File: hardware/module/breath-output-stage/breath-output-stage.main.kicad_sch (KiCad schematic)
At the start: 11 parts

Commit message: WIP module schematics: footprints, bought-part fields, and the two board projects (module-main, module-jack)
Recovered from a container restart; not yet exported or checked.

Co-Authored-By: Claude Opus 5.5 <noreply@anthropic.com>
Claude-Session: https://claude.ai/code/session_01LmB4muFXnoLprWX4JzuJ5A
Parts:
- C-DEC-BREATH-NEG, C-DEC-BREATH-POS: footprint (none) -> Capacitor_SMD:C_0805_2012Metric; Assembly (none) -> machine; LCSC (none) -> C49678; MPN (none) -> CC0805KRX7R9BB104; Manufacturer (none) -> YAGEO
- C-OUT-BREATH: footprint (none) -> Capacitor_SMD:C_1206_3216Metric; Assembly (none) -> machine; LCSC (none) -> C3774076; MPN (none) -> 50MU334MA23216; Manufacturer (none) -> Rubycon
- D-JACK-CLAMP: footprint (none) -> Package_TO_SOT_SMD:SOT-23; Assembly (none) -> machine; LCSC (none) -> C2500; MPN (none) -> BAV99,215; Manufacturer (none) -> Nexperia
- R-BREATH-FB: footprint (none) -> Resistor_SMD:R_0805_2012Metric; Assembly (none) -> machine; LCSC (none) -> C17678; MPN (none) -> 0805W8F4022T5E; Manufacturer (none) -> UNI-ROYAL(Uniroyal Elec)
- R-BREATH-IN: footprint (none) -> Resistor_SMD:R_0805_2012Metric; Assembly (none) -> machine; LCSC (none) -> C17414; MPN (none) -> 0805W8F1002T5E; Manufacturer (none) -> UNI-ROYAL(Uniroyal Elec)
- R-BREATH-OFF: footprint (none) -> Resistor_SMD:R_0805_2012Metric; Assembly (none) -> machine; LCSC (none) -> C17550; MPN (none) -> 0805W8F2102T5E; Manufacturer (none) -> UNI-ROYAL(Uniroyal Elec)
- R-BREATH-OFFNEG: footprint (none) -> Resistor_SMD:R_0805_2012Metric; Assembly (none) -> machine; LCSC (none) -> C17873; MPN (none) -> 0805W8F9532T5E; Manufacturer (none) -> UNI-ROYAL(Uniroyal Elec)
- R-GAIN-FLOOR: footprint (none) -> Resistor_SMD:R_0805_2012Metric; Assembly (none) -> machine; LCSC (none) -> C17806; MPN (none) -> 0805W8F7151T5E; Manufacturer (none) -> UNI-ROYAL(Uniroyal Elec)
- R-OUT-PROT: footprint (none) -> Resistor_SMD:R_1206_3216Metric; Assembly (none) -> machine; LCSC (none) -> C4261071; MPN (none) -> ERJ-P08F1001V; Manufacturer (none) -> Panasonic
- U-BREATH-OPA: footprint (none) -> Package_SO:SOIC-8_3.9x4.9mm_P1.27mm; Assembly (none) -> machine; LCSC (none) -> C139363; MPN (none) -> OPA2197IDR; Manufacturer (none) -> Texas Instruments

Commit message: #32: checkpoint — switchable breath band-limit, 1.5 kHz ADC filter, breath LED
Receive stage: C_diff switched by U-BW-SW (TMUX6112) from SW-BREATH-BW
(NKK M2024, left 500 Hz / centre 1.5 kHz / right WIDE): 680 pF fixed,
3.9 nF and 10 nF switched; C_cm 68 pF matched pair. C-OUT-BREATH 10 nF C0G.
C-AA-ADC 18 nF (1.47 kHz), sample rate kept at 4 kHz. Breath LED driver on
U-REF-BUF B. Sheets, BOM fragments, datasheets (TMUX6112, MMBT3904), sims,
ADR 0003/0004 amendments, pages. Sims still being re-run.

Gate-Red: sims stale while re-running (breath-receive-stage, breath-output-stage, interfaces/system, pitch-stage); breath-sense-link/sim pg_gain_max < 1e-3 fails in every mode and power-entry/sim led-pwm breath_mv fails at 2 kHz - both consequences of #32 left for the owner, not loosened; breath-receive-stage cmrr-wide fails 58.5 dB above ~7.4 kHz (owner); kicad: module-main and main-board .kicad_pcb parity broken by the new/changed parts (re-placement is the module re-layout's; pcb not touched), plus module-main's pre-existing routing failures

Co-Authored-By: Claude Opus 5.5 <noreply@anthropic.com>
Claude-Session: https://claude.ai/code/session_01LmB4muFXnoLprWX4JzuJ5A
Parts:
- C-OUT-BREATH: value 330nF film -> 10nF C0G; LCSC C3774076 -> C97928; MPN 50MU334MA23216 -> GRM3195C1H103JA01D; Manufacturer Rubycon -> Murata
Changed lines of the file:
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@@
     (in_bom yes) (on_board yes) (dnp no)
     (property "Reference" "C-OUT-BREATH" (at 43.18 232.41 0) (effects (font (size 1.27 1.27)) (justify left)))
-    (property "Value" "330nF film" (at 43.18 234.95 0) (effects (font (size 1.27 1.27)) (justify left)))
+    (property "Value" "10nF C0G" (at 43.18 234.95 0) (effects (font (size 1.27 1.27)) (justify left)))
     (property "Footprint" "Capacitor_SMD:C_1206_3216Metric" (at 41.91 237.49 0) (effects (font (size 1.27 1.27)) hide))
     (property "Datasheet" "" (at 40.64 233.68 0) (effects (font (size 1.27 1.27)) hide))
     (property "Row" "C-OUT-BREATH" (at 40.64 233.68 0) (effects (font (size 1.27 1.27)) hide))
     (property "Pins" "1=1 2=2" (at 40.64 233.68 0) (effects (font (size 1.27 1.27)) hide))
-    (property "Manufacturer" "Rubycon" (at 40.64 233.68 0) (effects (font (size 1.27 1.27)) hide))
-    (property "MPN" "50MU334MA23216" (at 40.64 233.68 0) (effects (font (size 1.27 1.27)) hide))
-    (property "LCSC" "C3774076" (at 40.64 233.68 0) (effects (font (size 1.27 1.27)) hide))
+    (property "Manufacturer" "Murata" (at 40.64 233.68 0) (effects (font (size 1.27 1.27)) hide))
+    (property "MPN" "GRM3195C1H103JA01D" (at 40.64 233.68 0) (effects (font (size 1.27 1.27)) hide))
+    (property "LCSC" "C97928" (at 40.64 233.68 0) (effects (font (size 1.27 1.27)) hide))
     (property "Assembly" "machine" (at 40.64 233.68 0) (effects (font (size 1.27 1.27)) hide))
     (pin "1")
@@
   (label "SUM_NODE" (at 81.28 53.34 180) (fields_autoplaced) (effects (font (size 1.27 1.27)) (justify right bottom)))
   (wire (pts (xy 99.06 50.8) (xy 101.6 50.8)) (stroke (width 0) (type default)))
-  (label "BREATH_OUT" (at 101.6 50.8 0) (fields_autoplaced) (effects (font (size 1.27 1.27)) (justify left bottom)))
+  (hierarchical_label "BREATH_OUT" (shape output) (at 101.6 50.8 0) (effects (font (size 1.27 1.27)) (justify left))
+    (property "Dir" "out" (at 101.6 50.8 0) (effects (font (size 1.27 1.27)) hide))
+    (property "To" "module/breath-receive-stage" (at 101.6 50.8 0) (effects (font (size 1.27 1.27)) hide))
+    (property "Note" "The summer's output inside its loop, ahead of R-OUT-PROT: the breath LED's driver reads it (#32)" (at 101.6 50.8 0) (effects (font (size 1.27 1.27)) hide)))
   (wire (pts (xy 345.44 191.77) (xy 345.44 194.31)) (stroke (width 0) (type default)))
-  (label "BREATH_OUT" (at 345.44 194.31 270) (fields_autoplaced) (effects (font (size 1.27 1.27)) (justify right bottom)))
+  (hierarchical_label "BREATH_OUT" (shape output) (at 345.44 194.31 270) (effects (font (size 1.27 1.27)) (justify right))
+    (property "Dir" "out" (at 345.44 194.31 0) (effects (font (size 1.27 1.27)) hide))
+    (property "To" "module/breath-receive-stage" (at 345.44 194.31 0) (effects (font (size 1.27 1.27)) hide))
+    (property "Note" "The summer's output inside its loop, ahead of R-OUT-PROT: the breath LED's driver reads it (#32)" (at 345.44 194.31 0) (effects (font (size 1.27 1.27)) hide)))
   (wire (pts (xy 421.64 193.04) (xy 421.64 195.58)) (stroke (width 0) (type default)))
-  (label "BREATH_OUT" (at 421.64 195.58 270) (fields_autoplaced) (effects (font (size 1.27 1.27)) (justify right bottom)))
+  (hierarchical_label "BREATH_OUT" (shape output) (at 421.64 195.58 270) (effects (font (size 1.27 1.27)) (justify right))
+    (property "Dir" "out" (at 421.64 195.58 0) (effects (font (size 1.27 1.27)) hide))
+    (property "To" "module/breath-receive-stage" (at 421.64 195.58 0) (effects (font (size 1.27 1.27)) hide))
+    (property "Note" "The summer's output inside its loop, ahead of R-OUT-PROT: the breath LED's driver reads it (#32)" (at 421.64 195.58 0) (effects (font (size 1.27 1.27)) hide)))
   (wire (pts (xy 497.84 184.15) (xy 497.84 181.61)) (stroke (width 0) (type default)))
-  (label "BREATH_OUT" (at 497.84 181.61 90) (fields_autoplaced) (effects (font (size 1.27 1.27)) (justify left bottom)))
+  (hierarchical_label "BREATH_OUT" (shape output) (at 497.84 181.61 90) (effects (font (size 1.27 1.27)) (justify left))
+    (property "Dir" "out" (at 497.84 181.61 0) (effects (font (size 1.27 1.27)) hide))
+    (property "To" "module/breath-receive-stage" (at 497.84 181.61 0) (effects (font (size 1.27 1.27)) hide))
+    (property "Note" "The summer's output inside its loop, ahead of R-OUT-PROT: the breath LED's driver reads it (#32)" (at 497.84 181.61 0) (effects (font (size 1.27 1.27)) hide)))
   (wire (pts (xy 497.84 191.77) (xy 497.84 194.31)) (stroke (width 0) (type default)))
   (hierarchical_label "JACK_TIP" (shape passive) (at 497.84 194.31 270) (effects (font (size 1.27 1.27)) (justify right))

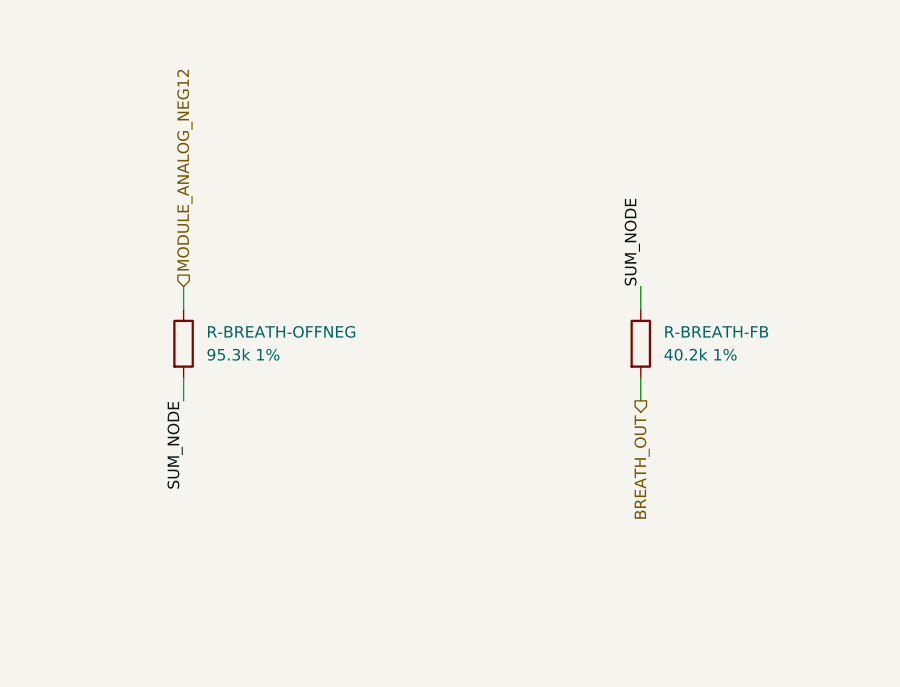
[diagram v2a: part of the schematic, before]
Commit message: #32: checkpoint - the owner's three answers and side-adjust trimmers
Owner decisions of 2026-10-04, recorded in ADR 0003/0004/0023/0024:
- WIDE's CMRR requirement band is DC to 7 kHz ("Keep 10 kHz, accept");
  cmrr-wide holds 58.5 dB there and records 10 kHz.
- D-TVS-BREATH is the PESD12VL1BA (19 pF), datasheet banked; PWR_GND
  held under -60 dB in each mode's band, WIDE at the accepted figure.
- The -12 V offset leg is filtered: R-BREATH-OFFNEG-A/-B 47.5k with
  C-BREATH-OFFNEG 1 uF at the split (6.7 Hz). Rest level +16 mV.
- The four trimmers are Bourns 3296X side-adjust, set with the module
  out of the rack; no rear-access windows. Current 3296 datasheet banked.

Sims are mid-run; their results land in the next commit.

Gate-Red: sim results stale or pre-change for receive-stage, power-entry, pitch-stage, mod-channels, shaper, system, breath-excitation-reference, digital-and-supervision and panel-led while they re-run on these inputs (checkpoint, as asked every 45 min); module-main and main-board .kicad_pcb parity with the new/changed parts (layout's, not touched here); main-board fab stale against the breath-adc sheet; module-main's existing routing/silk/acid-trap failures.

Co-Authored-By: Claude Opus 5.5 <noreply@anthropic.com>
Claude-Session: https://claude.ai/code/session_01LmB4muFXnoLprWX4JzuJ5A
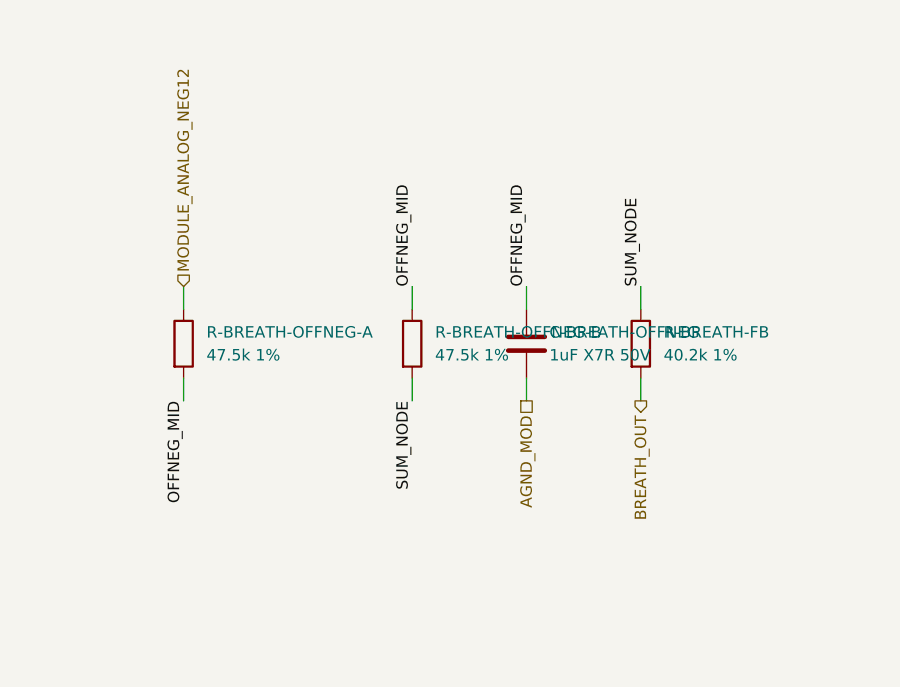
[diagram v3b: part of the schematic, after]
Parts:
- added C-BREATH-OFFNEG: 1uF X7R 50V, Capacitor_SMD:C_1206_3216Metric, symbol Device:C
- added R-BREATH-OFFNEG-B: 47.5k 1%, Resistor_SMD:R_0805_2012Metric, symbol Device:R
- R-BREATH-OFFNEG-A: renamed from R-BREATH-OFFNEG; value 95.3k 1% -> 47.5k 1%; LCSC C17873 -> C26011; MPN 0805W8F9532T5E -> 0805W8F4752T5E
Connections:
- net AGND_MOD: now also C-BREATH-OFFNEG.2
- net SUM_NODE: now also R-BREATH-OFFNEG-B.2; no longer R-BREATH-OFFNEG-A.2
- new net OFFNEG_MID: C-BREATH-OFFNEG.1, R-BREATH-OFFNEG-A.2, R-BREATH-OFFNEG-B.1
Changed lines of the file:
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@@
   (symbol (lib_id "Device:R") (at 294.64 187.96 0) (unit 1)
     (in_bom yes) (on_board yes) (dnp no)
-    (property "Reference" "R-BREATH-OFFNEG" (at 297.18 186.69 0) (effects (font (size 1.27 1.27)) (justify left)))
-    (property "Value" "95.3k 1%" (at 297.18 189.23 0) (effects (font (size 1.27 1.27)) (justify left)))
+    (property "Reference" "R-BREATH-OFFNEG-A" (at 297.18 186.69 0) (effects (font (size 1.27 1.27)) (justify left)))
+    (property "Value" "47.5k 1%" (at 297.18 189.23 0) (effects (font (size 1.27 1.27)) (justify left)))
     (property "Footprint" "Resistor_SMD:R_0805_2012Metric" (at 293.37 187.96 0) (effects (font (size 1.27 1.27)) hide))
     (property "Datasheet" "" (at 294.64 187.96 0) (effects (font (size 1.27 1.27)) hide))
@@
     (property "Drawn_as" "R-OFFNEG" (at 294.64 187.96 0) (effects (font (size 1.27 1.27)) hide))
     (property "Manufacturer" "UNI-ROYAL(Uniroyal Elec)" (at 294.64 187.96 0) (effects (font (size 1.27 1.27)) hide))
-    (property "MPN" "0805W8F9532T5E" (at 294.64 187.96 0) (effects (font (size 1.27 1.27)) hide))
-    (property "LCSC" "C17873" (at 294.64 187.96 0) (effects (font (size 1.27 1.27)) hide))
+    (property "MPN" "0805W8F4752T5E" (at 294.64 187.96 0) (effects (font (size 1.27 1.27)) hide))
+    (property "LCSC" "C26011" (at 294.64 187.96 0) (effects (font (size 1.27 1.27)) hide))
     (property "Assembly" "machine" (at 294.64 187.96 0) (effects (font (size 1.27 1.27)) hide))
     (pin "1")
     (pin "2")
-    (instances (project "module-main" (path "/fc77e9f9-9171-5c83-92ae-8cafe880764e/17312cee-ca35-5de4-93d5-247b1fad2ee3" (reference "R24") (unit 1))) (project "breath-output-stage.main" (path "/1628897f-2ed0-5a6a-9bf2-749dfca7ac5c" (reference "R-BREATH-OFFNEG") (unit 1))) (project "breath-output-stage" (path "/6f4edadb-6257-58e5-9d51-bec8cbdf5df0/ec51b1d2-0ca2-56b1-b291-6e590255992a" (reference "R-BREATH-OFFNEG") (unit 1))))
+    (instances (project "module-main" (path "/fc77e9f9-9171-5c83-92ae-8cafe880764e/17312cee-ca35-5de4-93d5-247b1fad2ee3" (reference "R24") (unit 1))) (project "breath-output-stage.main" (path "/1628897f-2ed0-5a6a-9bf2-749dfca7ac5c" (reference "R-BREATH-OFFNEG-A") (unit 1))) (project "breath-output-stage" (path "/6f4edadb-6257-58e5-9d51-bec8cbdf5df0/ec51b1d2-0ca2-56b1-b291-6e590255992a" (reference "R-BREATH-OFFNEG-A") (unit 1))))
   )
   (symbol (lib_id "Device:R") (at 345.44 187.96 0) (unit 1)
@@
   (label "SUM_NODE" (at 243.84 194.31 270) (fields_autoplaced) (effects (font (size 1.27 1.27)) (justify right bottom)))
   (wire (pts (xy 294.64 191.77) (xy 294.64 194.31)) (stroke (width 0) (type default)))
-  (label "SUM_NODE" (at 294.64 194.31 270) (fields_autoplaced) (effects (font (size 1.27 1.27)) (justify right bottom)))
+  (label "OFFNEG_MID" (at 294.64 194.31 270) (fields_autoplaced) (effects (font (size 1.27 1.27)) (justify right bottom)))
   (wire (pts (xy 345.44 184.15) (xy 345.44 181.61)) (stroke (width 0) (type default)))
   (label "SUM_NODE" (at 345.44 181.61 90) (fields_autoplaced) (effects (font (size 1.27 1.27)) (justify left bottom)))
@@
     (property "Dir" "ref" (at 142.24 194.31 0) (effects (font (size 1.27 1.27)) hide))
     (property "From" "module/power-entry" (at 142.24 194.31 0) (effects (font (size 1.27 1.27)) hide)))
+  (symbol (lib_id "Device:R") (at 320.04 187.96 0) (unit 1)
+    (in_bom yes) (on_board yes) (dnp no)
+    (property "Reference" "R-BREATH-OFFNEG-B" (at 322.58 186.69 0) (effects (font (size 1.27 1.27)) (justify left)))
+    (property "Value" "47.5k 1%" (at 322.58 189.23 0) (effects (font (size 1.27 1.27)) (justify left)))
+    (property "Footprint" "Resistor_SMD:R_0805_2012Metric" (at 318.77 187.96 0) (effects (font (size 1.27 1.27)) hide))
+    (property "Datasheet" "" (at 320.04 187.96 0) (effects (font (size 1.27 1.27)) hide))
+    (property "Row" "R-BREATH-OFFNEG" (at 320.04 187.96 0) (effects (font (size 1.27 1.27)) hide))
+    (property "Pins" "1=1 2=2" (at 320.04 187.96 0) (effects (font (size 1.27 1.27)) hide))
+    (property "Drawn_as" "R-OFFNEG" (at 320.04 187.96 0) (effects (font (size 1.27 1.27)) hide))
+    (property "Note" "The second half of the offset's -12 V leg (#32, owner 2026-10-04: 'Add RC filter (Recommended)'): R-BREATH-OFFNEG-A from -12 V to OFFNEG_MID, this from OFFNEG_MID to the summing node, C-BREATH-OFFNEG from OFFNEG_MID to the star. 2 x 47.5k for the 95.3k it replaces" (at 320.04 187.96 0) (effects (font (size 1.27 1.27)) hide))
+    (property "Pins_source" "Device:R, two-terminal: pin 1 and pin 2 are interchangeable" (at 320.04 187.96 0) (effects (font (size 1.27 1.27)) hide))
+    (property "Manufacturer" "UNI-ROYAL(Uniroyal Elec)" (at 320.04 187.96 0) (effects (font (size 1.27 1.27)) hide))
+    (property "MPN" "0805W8F4752T5E" (at 320.04 187.96 0) (effects (font (size 1.27 1.27)) hide))
+    (property "LCSC" "C26011" (at 320.04 187.96 0) (effects (font (size 1.27 1.27)) hide))
+    (property "Assembly" "machine" (at 320.04 187.96 0) (effects (font (size 1.27 1.27)) hide))
+    (pin "1")
+    (pin "2")
+    (instances (project "breath-output-stage.main" (path "/1628897f-2ed0-5a6a-9bf2-749dfca7ac5c" (reference "R-BREATH-OFFNEG-B") (unit 1))) (project "module-main" (path "/fc77e9f9-9171-5c83-92ae-8cafe880764e/17312cee-ca35-5de4-93d5-247b1fad2ee3" (reference "R82") (unit 1))) (project "breath-output-stage" (path "/6f4edadb-6257-58e5-9d51-bec8cbdf5df0/ec51b1d2-0ca2-56b1-b291-6e590255992a" (reference "R-BREATH-OFFNEG-B") (unit 1))))
+  )
+  (wire (pts (xy 320.04 184.15) (xy 320.04 181.61)) (stroke (width 0) (type default)))
+  (label "OFFNEG_MID" (at 320.04 181.61 90) (fields_autoplaced) (effects (font (size 1.27 1.27)) (justify left bottom)))
+  (wire (pts (xy 320.04 191.77) (xy 320.04 194.31)) (stroke (width 0) (type default)))
+  (label "SUM_NODE" (at 320.04 194.31 270) (fields_autoplaced) (effects (font (size 1.27 1.27)) (justify right bottom)))
+  (symbol (lib_id "Device:C") (at 332.74 187.96 0) (unit 1)
+    (in_bom yes) (on_board yes) (dnp no)
+    (property "Reference" "C-BREATH-OFFNEG" (at 335.28 186.69 0) (effects (font (size 1.27 1.27)) (justify left)))
+    (property "Value" "1uF X7R 50V" (at 335.28 189.23 0) (effects (font (size 1.27 1.27)) (justify left)))
+    (property "Footprint" "Capacitor_SMD:C_1206_3216Metric" (at 334.01 191.77 0) (effects (font (size 1.27 1.27)) hide))
+    (property "Datasheet" "" (at 332.74 187.96 0) (effects (font (size 1.27 1.27)) hide))
+    (property "Row" "C-BREATH-OFFNEG" (at 332.74 187.96 0) (effects (font (size 1.27 1.27)) hide))
+    (property "Pins" "1=1 2=2" (at 332.74 187.96 0) (effects (font (size 1.27 1.27)) hide))
+    (property "Note" "Filters the -12 V rail out of the breath offset (#32): 1/(2 pi x 23.75 kohm x 1 uF) = 6.7 Hz, so the LED row's 2-4 kHz PWM and the rail's breath-rate movement are taken down before the summer. Returns to the star. X7R 50 V in 1206 so 6 V of DC bias costs little; a 1206 C0G at 1 uF is not stocked" (at 332.74 187.96 0) (effects (font (size 1.27 1.27)) hide))
+    (property "Pins_source" "Device:C, two-terminal: pin 1 and pin 2 are interchangeable" (at 332.74 187.96 0) (effects (font (size 1.27 1.27)) hide))
+    (property "Manufacturer" "Samsung Electro-Mechanics" (at 332.74 187.96 0) (effects (font (size 1.27 1.27)) hide))
+    (property "MPN" "CL31B105KBHNNNE" (at 332.74 187.96 0) (effects (font (size 1.27 1.27)) hide))
+    (property "LCSC" "C1848" (at 332.74 187.96 0) (effects (font (size 1.27 1.27)) hide))
+    (property "Assembly" "machine" (at 332.74 187.96 0) (effects (font (size 1.27 1.27)) hide))
+    (pin "1")
+    (pin "2")
+    (instances (project "breath-output-stage.main" (path "/1628897f-2ed0-5a6a-9bf2-749dfca7ac5c" (reference "C-BREATH-OFFNEG") (unit 1))) (project "module-main" (path "/fc77e9f9-9171-5c83-92ae-8cafe880764e/17312cee-ca35-5de4-93d5-247b1fad2ee3" (reference "C58") (unit 1))) (project "breath-output-stage" (path "/6f4edadb-6257-58e5-9d51-bec8cbdf5df0/ec51b1d2-0ca2-56b1-b291-6e590255992a" (reference "C-BREATH-OFFNEG") (unit 1))))
+  )
+  (wire (pts (xy 332.74 184.15) (xy 332.74 181.61)) (stroke (width 0) (type default)))
+  (label "OFFNEG_MID" (at 332.74 181.61 90) (fields_autoplaced) (effects (font (size 1.27 1.27)) (justify left bottom)))
+  (wire (pts (xy 332.74 191.77) (xy 332.74 194.31)) (stroke (width 0) (type default)))
+  (hierarchical_label "AGND_MOD" (shape passive) (at 332.74 194.31 270) (effects (font (size 1.27 1.27)) (justify right))
+    (property "Dir" "ref" (at 332.74 194.31 0) (effects (font (size 1.27 1.27)) hide))
+    (property "From" "module/power-entry" (at 332.74 194.31 0) (effects (font (size 1.27 1.27)) hide)))
   (sheet_instances (path "/" (page "1")))
 )
